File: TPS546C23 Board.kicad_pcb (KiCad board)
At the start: 2 copper layers, 35 parts, among them IC1 TPS546C23RVFT

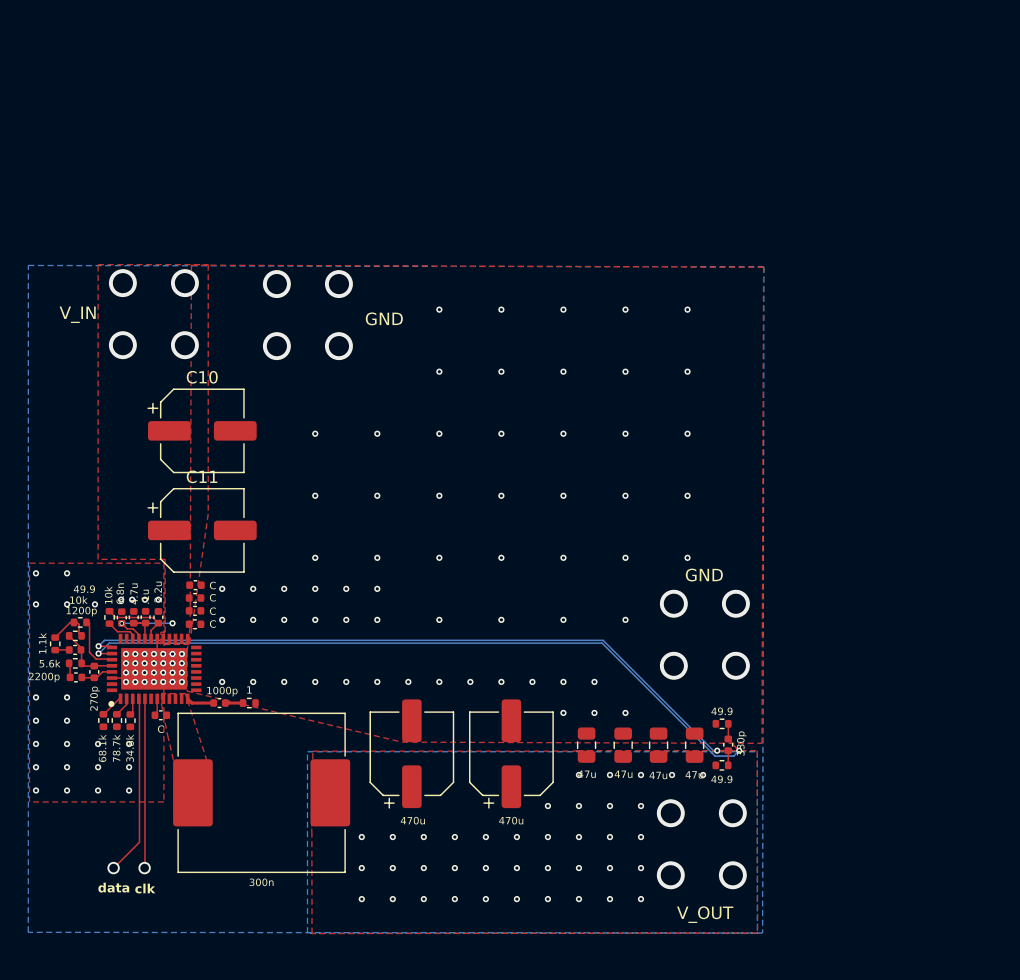
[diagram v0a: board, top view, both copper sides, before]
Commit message: add fp and sym, it wasnt final
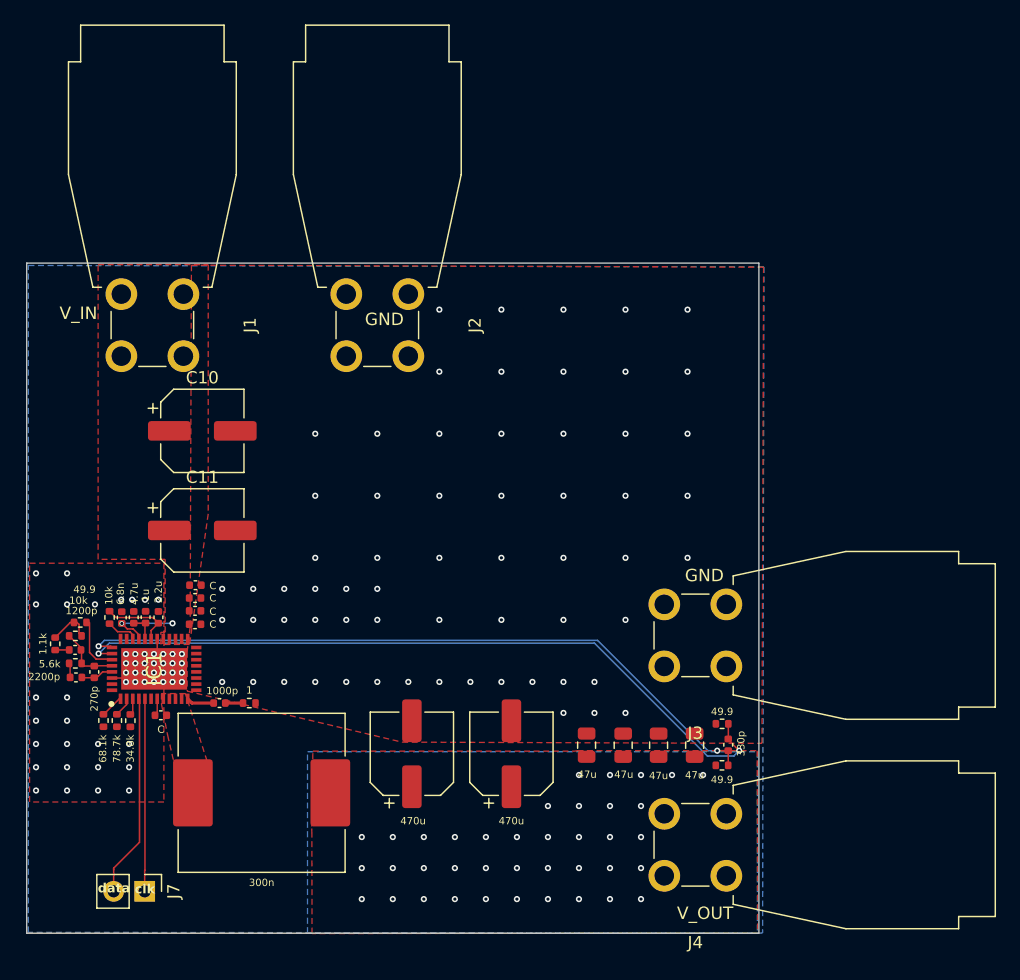
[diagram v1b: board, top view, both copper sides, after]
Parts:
- added J1: Conn_01x01, Custom:CalTest_CT3151, F.Cu at (207.6, 39.4)
- added J2: Conn_01x01, Custom:CalTest_CT3151, F.Cu at (226.1, 39.4)
- added J3: Conn_01x01, Custom:CalTest_CT3151, F.Cu at (252.1, 69.8)
- added J4: Conn_01x01, Custom:CalTest_CT3151, F.Cu at (252.1, 87.0)
- added J7: Conn_01x02_Pin, Connector_PinHeader_2.54mm:PinHeader_1x02_P2.54mm_Vertical, F.Cu at (204.5, 88.3)
- IC1: footprint LIB_TPS546C23RVFT:QFN50P500X700X152-41N-D -> Custom:QFN50P500X700X152-41N-D
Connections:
- IC1 pad 40: CNTL -> unconnected-(IC1-CNTL-Pad40)
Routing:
- net Data: track 14.9 -> 16.7 mm, vias 1 -> 0
- net CLK: track 14.0 -> 15.8 mm, vias 1 -> 0
- net V_sdec: vias 6 -> 2
- net V_A: vias 47 -> 39
- net AGND: vias 124 -> 116
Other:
- board outline added: 59.9 x 54.9 mm
